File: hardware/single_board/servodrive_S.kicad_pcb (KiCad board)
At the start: 6 copper layers, 65 x 65 mm, 195 parts, among them J1 PhasePad_Arc, J12 USB-C, J13 EXPANSION, J14 RS485 IN, J15 RS485 OUT, J2 PhasePad_Arc, J3 PhasePad_Arc, J4 BusPad_Arc, J5 BusPad_Arc, Q1 BSC030N08NS5, Q1001 2N7002, Q2 BSC030N08NS5, Q3 BSC030N08NS5, Q4 BSC030N08NS5, Q5 BSC030N08NS5, Q6 BSC030N08NS5, SW1 BOOTSEL, U1 EG2103, U10 MT6701, U11 LMR38010SDDAR, U12 LMR38010SDDAR, U13 USBLC6-2SC6, U14 SIT3088ETK, U15 SIT3088ETK, U17 SIT3088ETK, U18 SIT3088ETK, U2 EG2103, U3 EG2103, U4 INA241A3, U5 INA241A3, U6 INA241A3, U7 RP2350A, U8 W25Q128JVUXIQ, U9 SPX3819M5-3.3, Y1 12MHz

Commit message: Every placed part gets an LCSC number; 3D inductors and part colours fixed
LCSC (hardware/parts/lcsc.csv, 76 rows): every part the assembler places on
boards A (120) and S (173) now has a number, joined into the 3D part pane.
Chosen from the sister board's BOM where it had the part, JLC basic parts
where the rating allowed, each matched to the net it sits on and checked
against JLCPCB's library (model, package, rating, stock) on 2026-09-24. The
notes say why where it was not obvious: 100 V X7R/C0G on VBUS, 0.1% thin
film for the dividers, a Vishay WSL metal-strip jumper for phase C's 0R
(75 A, where a thick-film 0R carries a few), a CL 20 pF crystal for the
27 pF caps, the RGB LED placed rotated 180 deg. export_3d.py warns about any
placed part without a number; copper features (lands, lead pads, bosses)
get no LCSC row in the pane.

Two values changed because nothing stocked matches them:
- Shunts 1m6 -> 2m0 (WSLP20102L000FEA): no 1.6 mOhm 2010 exists at LCSC or
  JLCPCB. The pair is 1.0 mOhm, 50 mV/A, +-29.0 A worst case -- 2.5% over
  the 28.3 A peak, the margin draft 0.3 turned down, taken knowingly.
  geometry.SHUNT_EACH follows; spec, README and status page re-derive the
  sense chain and the loss budget (10.72 W, <= 6.67 K/W, >= 100 cm2).
- Flash W25Q128 -> W25Q16JVUXIQ: no 128 Mbit part comes in USON 2x3; this
  is the RP2350 reference design's part. Derived symbol renamed W25Q16JV.
Schematics regenerated in a scratch copy and only the changed sheets copied
back (diffed: nothing else moved); the routed boards' value fields patched
in place. ERC 0 and DRC 0 on both; KiCad's parity list is HEAD's minus one
(board A's U8 value mismatch). Board S's plan drawings and parts table
regenerated, which also brings them back in line with the final placement.

3D export:
- Board S's two buck inductors were invisible: kicad-cli 9.0.8 meshes a STEP
  that is an assembly of sub-assemblies (KiCad's own SWPA4030S) as empty
  nodes, silently. tools/flatten_step.py flattens it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
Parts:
- R105, R106, R205, R206: value 1m6 -> 2m0
- U8: value W25Q128JVUXIQ -> W25Q16JVUXIQ
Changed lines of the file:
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@@
 			)
 		)
-		(property "Value" "W25Q128JVUXIQ"
+		(property "Value" "W25Q16JVUXIQ"
 			(at 0 1.95 0)
 			(layer "F.Fab")
@@
 			)
 		)
-		(property "Value" "1m6"
+		(property "Value" "2m0"
 			(at 0 -2.280002 0)
 			(layer "B.Fab")
@@
 			)
 		)
-		(property "servodrive_role" "inline shunt, parallel pair - desolder one for the 18 A mode"
+		(property "servodrive_role" "inline shunt, parallel pair - desolder one for the 14.5 A mode"
 			(at 0 0 0)
 			(layer "B.Fab")
@@
 			)
 		)
-		(property "Value" "1m6"
+		(property "Value" "2m0"
 			(at 0 -2.28 0)
 			(layer "B.Fab")
@@
 			)
 		)
-		(property "servodrive_role" "inline shunt, parallel pair - desolder one for the 18 A mode"
+		(property "servodrive_role" "inline shunt, parallel pair - desolder one for the 14.5 A mode"
 			(at 0 0 0)
 			(layer "B.Fab")
@@
 			)
 		)
-		(property "Value" "1m6"
+		(property "Value" "2m0"
 			(at 0 -2.28 0)
 			(layer "B.Fab")
@@
 			)
 		)
-		(property "servodrive_role" "inline shunt, parallel pair - desolder one for the 18 A mode"
+		(property "servodrive_role" "inline shunt, parallel pair - desolder one for the 14.5 A mode"
 			(at 0 0 0)
 			(layer "B.Fab")
@@
 			)
 		)
-		(property "Value" "1m6"
+		(property "Value" "2m0"
 			(at 0 -2.280002 0)
 			(layer "B.Fab")
@@
 			)
 		)
-		(property "servodrive_role" "inline shunt, parallel pair - desolder one for the 18 A mode"
+		(property "servodrive_role" "inline shunt, parallel pair - desolder one for the 14.5 A mode"
 			(at 0 0 0)
 			(layer "B.Fab")

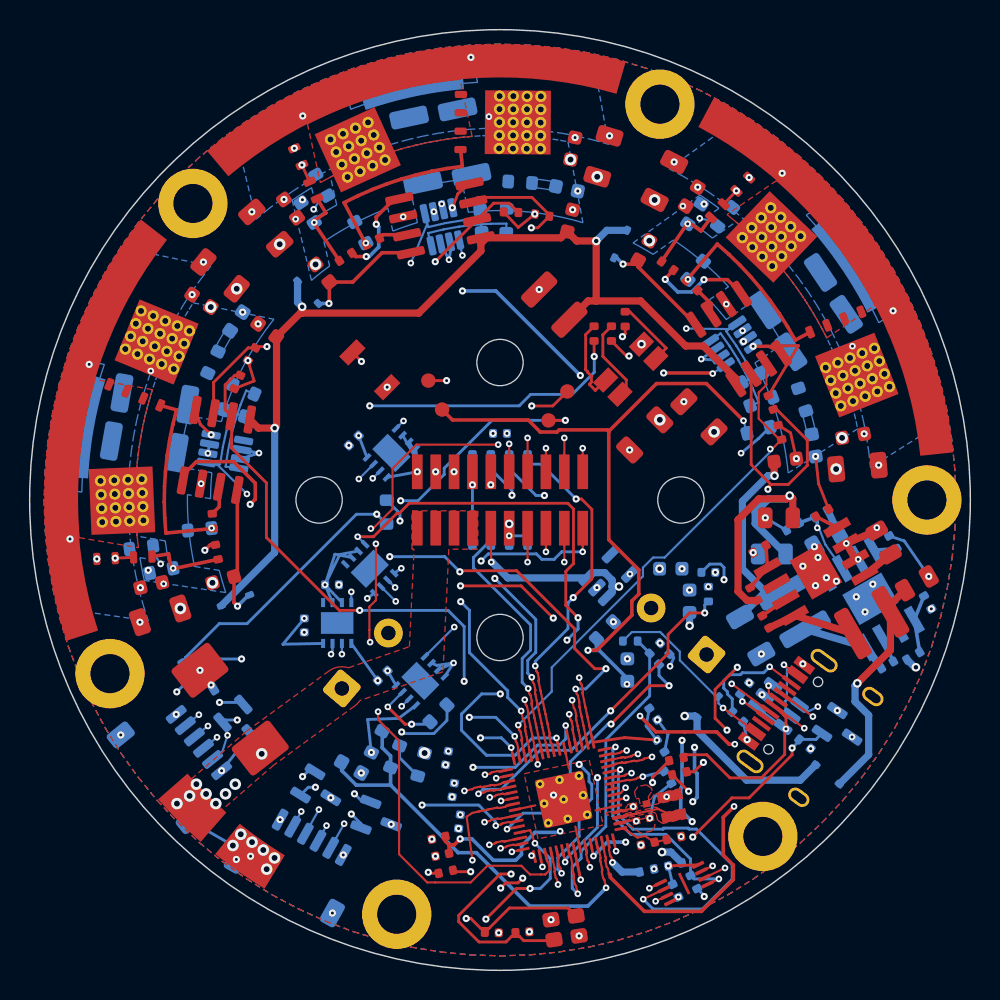
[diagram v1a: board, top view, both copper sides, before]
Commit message: Board S: bus on an XT30, set back from the edge; SIT3088s tidied; re-routed
J4 is now the rp2350-motor-controller's XT30 (AMASS XT30PW-M, C431092,
pin 1 GND, pin 2 VMOT) in place of the two bus pads. At the rim its pegs
land on both RS-485 ports and no other rim takes a JST SH, so it sits 5 mm
back with the plug's path kept clear; its pins land at R 14.5.

- placement_s: bus="xt30" arrangement; the XT30 placed by its body with a
  peg rule; C1001 to 135 deg; SMDJ54A under the XT30; SM712 stacks; the four
  SIT3088 turned alike facing the ports (put_rigid, pair) with their escape
  strips kept clear; divider as one row; SPINE keepout
- gen_boards: project copy of the XT30 footprint with its courtyard round
  the part; In2 tab over the VMOT pin; spine from it to the header; In2
  no-via fences over the narrow VBUS fingers (a route cut C1007's)
- fanout.pin_field: via fields round the XT30 pins; finish.py honours via
  keepouts on any layer
- P5S re-run with the XT30's bus current: 0.009-0.016 deg alone
- routed: 1913 segments, 411 vias, 0 unconnected, DRC/ERC/netlist clean
- single.html: the XT30 section; "Where it is" below the viewer

Co-Authored-By: Claude Opus 5.5 (1M context) <noreply@anthropic.com>
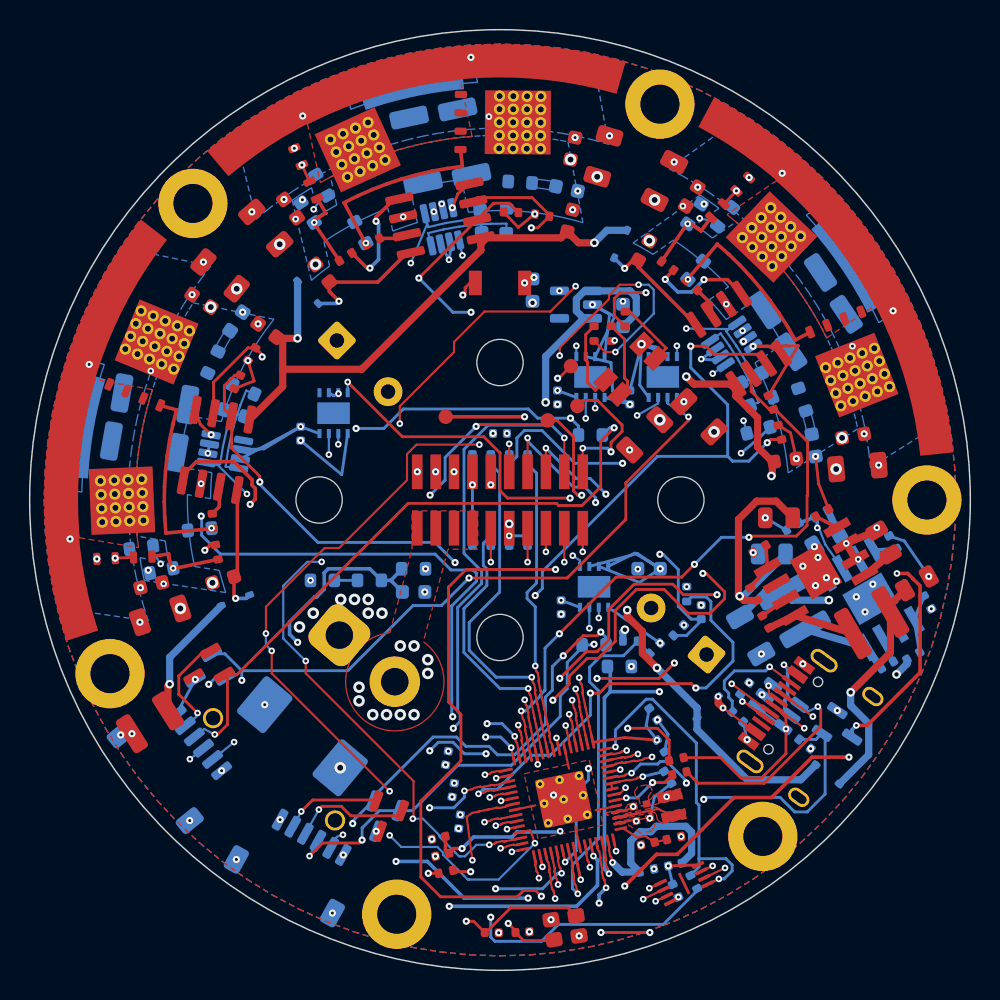
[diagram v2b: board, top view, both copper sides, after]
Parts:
- removed J5: BusPad_Arc, servodrive:BusPad_Arc
- D1001: moved to B.Cu
- D1102, D1105: moved to F.Cu
- J4: value BusPad_Arc -> XT30; footprint servodrive:BusPad_Arc -> servodrive:AMASS_XT30PW-M_1x02_P2.50mm_Horizontal
- moved C1009 40.2 mm to (123.8, 120.4), turned to -147.583 degrees
- moved C1104 24.3 mm to (157.0, 97.9), turned to -90 degrees
- moved U17 24.2 mm to (159.2, 96.5), turned to 0 degrees
- moved C1001 24.0 mm to (136.7, 94.0), turned to -45 degrees
- moved C712 21.5 mm to (150.2, 90.5), turned to 90 degrees
- moved C713 20.3 mm to (156.5, 92.2)
- moved U9 18.9 mm to (153.2, 91.5), turned to 180 degrees
- moved J4 15.6 mm to (136.9, 114.3), turned to 140 degrees
- moved R1106 15.1 mm to (154.2, 100.5), turned to 180 degrees
- moved U18 14.7 mm to (154.2, 96.5), turned to 0 degrees
- moved U15 14.5 mm to (136.5, 99.0)
- moved R801 14.4 mm to (135.7, 110.6), turned to 0 degrees
- moved C1105 14.4 mm to (152.0, 97.9), turned to -90 degrees
- moved U14 13.6 mm to (154.5, 111.0), turned to 0 degrees
- moved C1103 13.3 mm to (134.2, 100.4)
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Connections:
- J4 pad 1: VBUS -> GND
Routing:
- net RS485_OUT_DN_N: track 21.9 -> 72.4 mm
- net LED_B: track 47.6 -> 83.9 mm, vias 2 -> 4
- net HIN_A: track 75.7 -> 42.3 mm, vias 3 -> 4
- net RS485_OUT_DN_P: track 21.4 -> 51.5 mm, vias 3 -> 4
- net +5V: track 40.1 -> 67.5 mm
- net RS485_IN_UP_P: track 15.5 -> 37.7 mm, vias 3 -> 2
- net RS485_IN_UP_N: track 14.7 -> 36.1 mm, vias 3 -> 2
- net VBUS_SENSE: track 30.4 -> 51.3 mm, vias 1 -> 5
- net RS485_OUT_UP_P: track 29.0 -> 46.0 mm, vias 4 -> 3
- net RS485_IN_RX: track 32.9 -> 17.2 mm, vias 4 -> 2
- net GND: track 86.1 -> 101.8 mm, vias 121 -> 118
- net RS485_OUT_UP_N: track 36.0 -> 51.5 mm
- net FET_TEMP: track 85.6 -> 70.1 mm, vias 6 -> 5
- net GATE_OFF: track 39.0 -> 54.4 mm
- net EXP_GP22: track 30.6 -> 45.6 mm, vias 2 -> 4
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
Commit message: Board S: screw keepouts, finer In3 centre rules, encoder on SPI0 (WIP, unrouted)
Work in progress from 2026-09-24/25, saved before routing is finished.
The board file here is the generator's output, not a routed board.

- Keepouts on F.Cu and B.Cu round the four centre motor screws
- USB-C placed tangent to the edge
- Encoder on SPI0 (ENC_DO GPIO4, ENC_SCK GPIO6); J13 pins swapped
- C901 moved north; encoder stitching vias back in the chip's pads
- "fine centre" rule area: signal nets on In3 inside R 17 may use
  0.12 mm track and clearance (servodrive_S.kicad_dru); finish.py's
  maze tries 0.12 there when 0.15 fails; the area is stripped before
  the DSN export so freerouting doesn't see it as a keepout
- Footprint tweaks: 0402 small pads, L_pol_2016, RP2350 QFN

Co-Authored-By: Claude Opus 5.5 (1M context) <noreply@anthropic.com>
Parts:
- moved C1004 18.9 mm to (165.8, 117.8), turned to -135 degrees
- moved R1003 12.9 mm to (166.0, 118.1), turned to -15 degrees
- moved R1002 12.7 mm to (165.5, 108.1), turned to 75 degrees
- moved R1001 12.5 mm to (168.6, 106.1), turned to 165 degrees
- moved R1008 12.2 mm to (164.1, 113.1), turned to -105 degrees
- moved R1004 11.9 mm to (168.1, 118.7), turned to -15 degrees
- moved C603 11.4 mm to (176.6, 112.4), turned to -105 degrees
- moved C1011 11.2 mm to (175.2, 116.2), turned to -45 degrees
- moved C1005 10.2 mm to (170.4, 107.2), turned to -15 degrees
- moved D1003 9.83 mm to (171.9, 114.2), turned to -21.083 degrees
- moved C1003 9.30 mm to (167.3, 116.5), turned to -15 degrees
- moved Q1001 7.36 mm to (164.2, 120.8), turned to 45.73 degrees
- moved R1005 5.91 mm to (163.5, 123.8), turned to -50.538 degrees
- moved L1001 5.64 mm to (173.5, 110.4), turned to -15 degrees
- moved U11 5.61 mm to (168.0, 111.4), turned to 75 degrees
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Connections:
- J13 pad 11: +3V3 -> EXP_GP24
- J13 pad 12: RUN -> +5V
- J13 pad 14: EXP_GP24 -> +3V3
- J13 pad 9: +5V -> RUN
- U7 pad 7: ENC_SCK -> ENC_DO
- U7 pad 9: ENC_DO -> ENC_SCK
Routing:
- net +12V: track 126.1 -> 0.00 mm, vias 7 -> 0
- net LED_B: track 83.9 -> 1.56 mm, vias 4 -> 1
- net LED_R: track 78.7 -> 1.70 mm, vias 9 -> 1
- net RS485_OUT_DN_N: track 72.4 -> 2.66 mm, vias 3 -> 2
- net FET_TEMP: track 70.1 -> 3.17 mm, vias 5 -> 2
- net +5V: track 67.5 -> 1.93 mm, vias 4 -> 1
- net ISENSE_B: track 66.2 -> 1.91 mm, vias 3 -> 2
- net BOOTSEL: track 64.1 -> 0.00 mm, vias 2 -> 0
- net LED_G: track 66.3 -> 2.26 mm, vias 7 -> 1
- net RUN: track 63.6 -> 3.16 mm, vias 4 -> 2
- net ISENSE_A: track 61.5 -> 2.65 mm, vias 4 -> 2
- net LIN_C: track 58.9 -> 0.82 mm, vias 4 -> 1
- net SWCLK: track 61.8 -> 3.89 mm, vias 7 -> 2
- net GATE_OFF: track 54.4 -> 3.20 mm, vias 3 -> 1
- net RS485_OUT_UP_N: track 51.5 -> 2.70 mm, vias 4 -> 2
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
